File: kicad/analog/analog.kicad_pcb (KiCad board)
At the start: 4 copper layers, 75 x 50 mm, 85 parts, among them J101 FCI 20021221-00014T4LF, J301 CONN_02X05, Q201 DMG3414U, Q501 DMG3414U, Q601 DMG3414U, Q701 DMG3414U, U101 NCP694-3.3, U201 LTC2052, U202 ADS1220, U301 SP3003-04, U401 REF5030, U501 LTC2052, U502 ADS1220, U601 LTC2052, U602 ADS1220, U701 LTC2052, U702 ADS1220

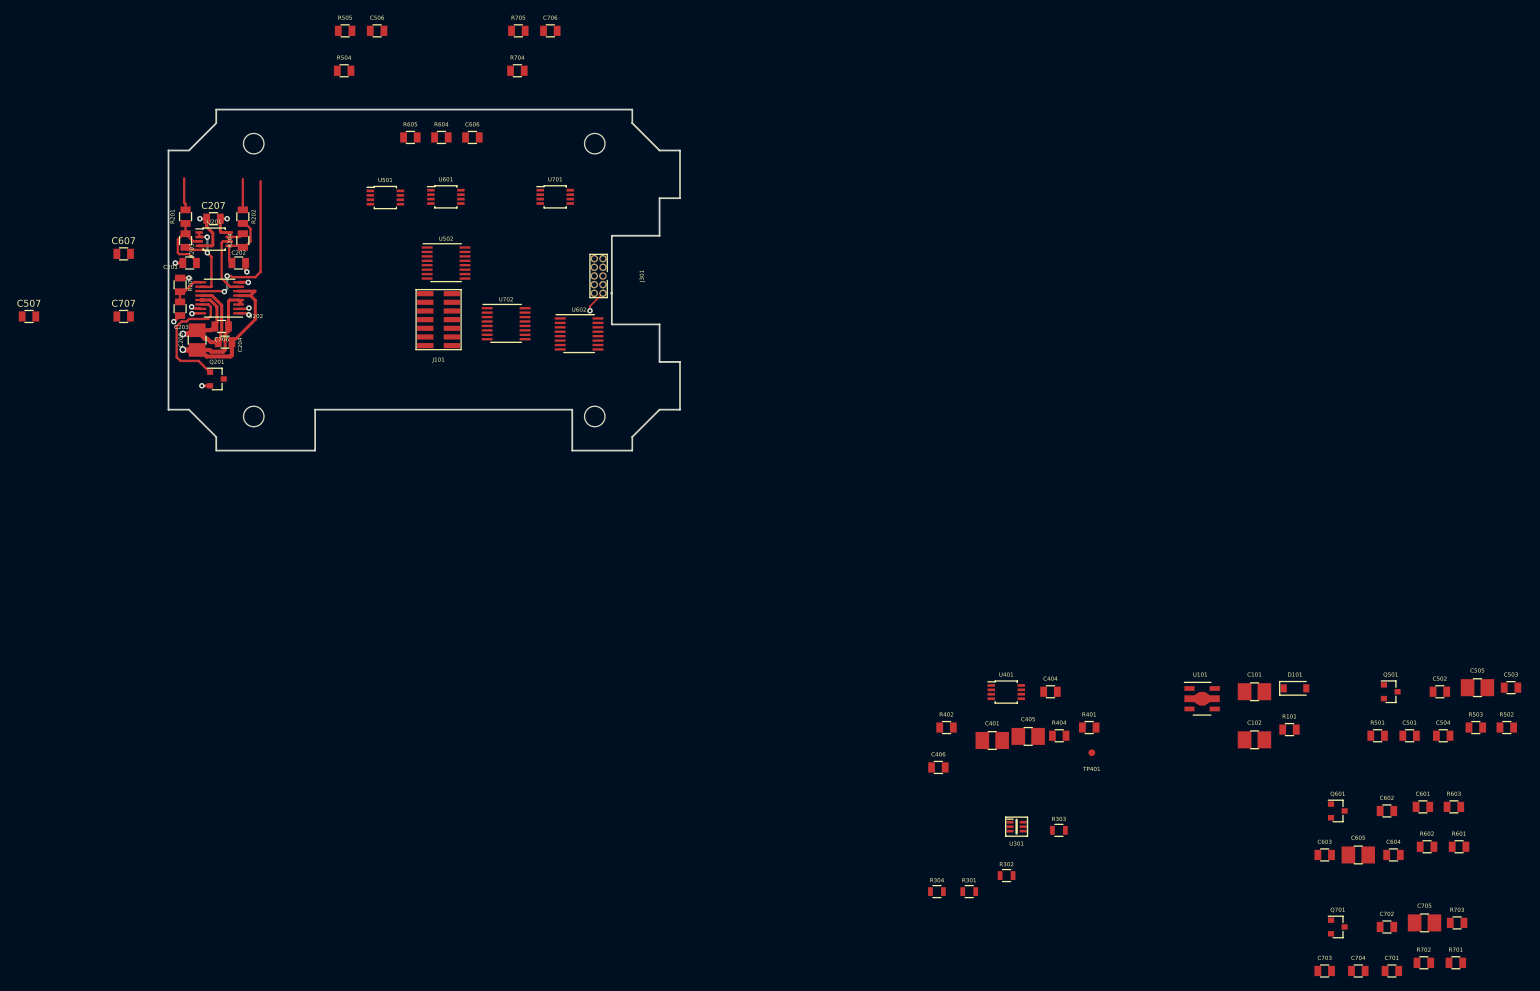
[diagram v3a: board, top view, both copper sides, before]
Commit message: analog routed DRC passes
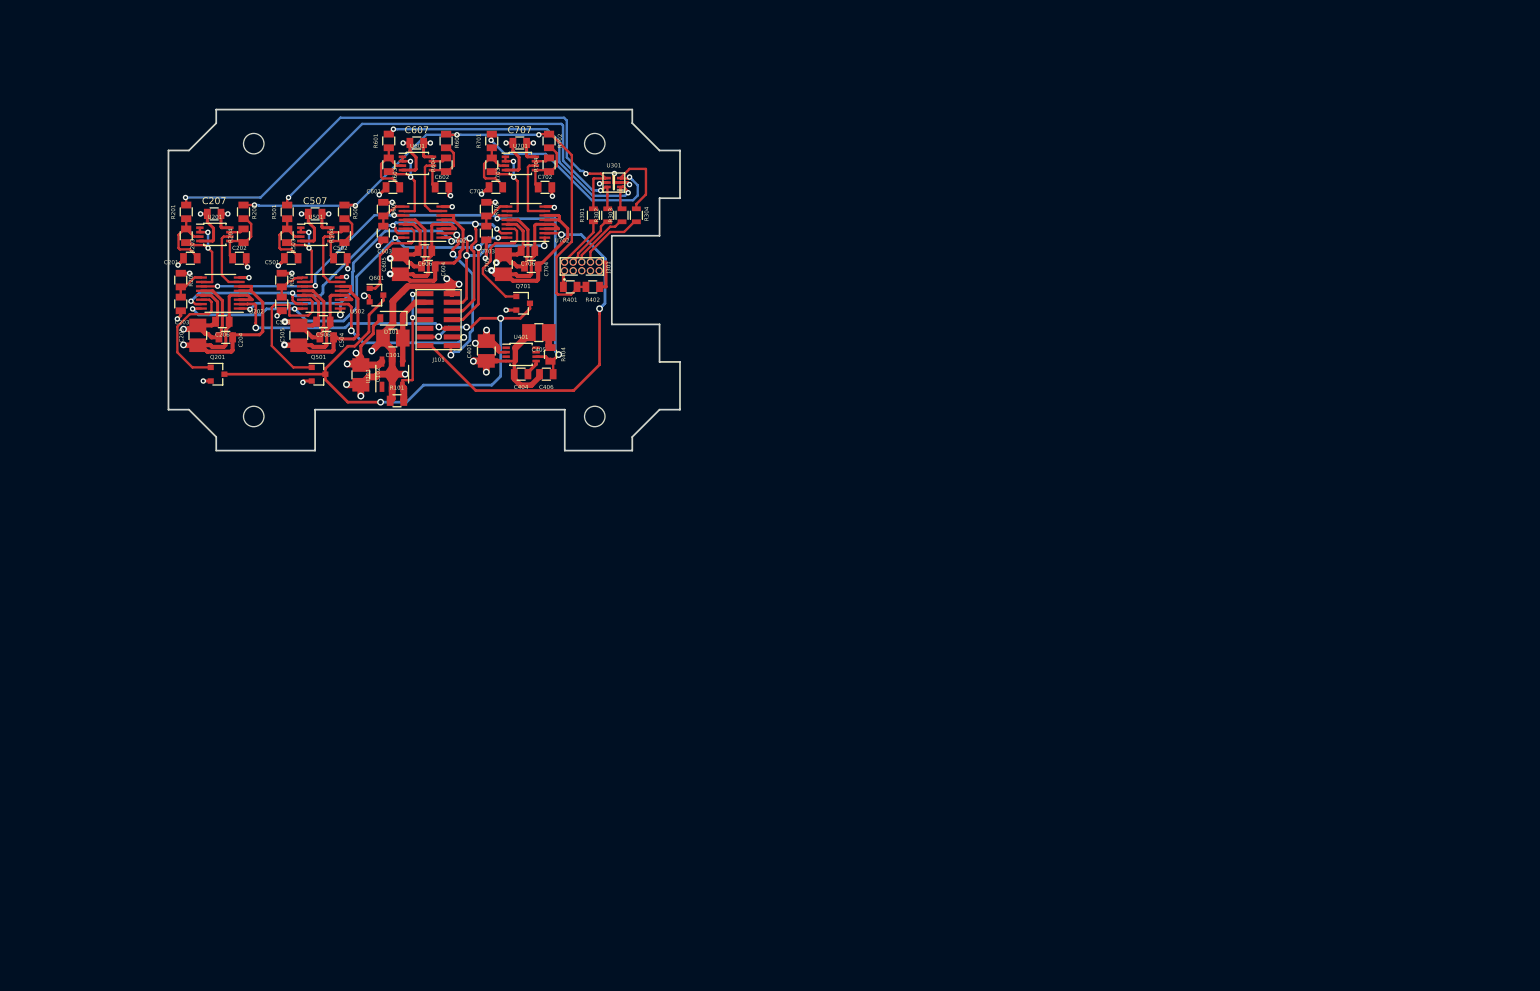
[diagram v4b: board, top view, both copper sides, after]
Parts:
- removed TP401: VREF, paddle:tp_th_1mm
- moved C503 188.8 mm to (16.6, 28.5), turned to 270 degrees
- moved R503 188.6 mm to (17.4, 18.5), turned to 270 degrees
- moved R601 188.0 mm to (32.3, 4.60), turned to 90 degrees
- moved R502 186.4 mm to (25.8, 15.0), turned to 90 degrees
- moved R701 185.7 mm to (47.4, 4.60), turned to 90 degrees
- moved R603 182.3 mm to (32.3, 8.10), turned to 270 degrees
- moved C505 180.4 mm to (19.1, 33.1), turned to 270 degrees
- moved R703 180.0 mm to (47.4, 8.10), turned to 270 degrees
- moved C501 178.3 mm to (18.0, 21.8)
- moved R501 177.4 mm to (17.4, 15.0), turned to 90 degrees
- moved R602 177.2 mm to (40.7, 4.60), turned to 90 degrees
- moved C601 176.2 mm to (32.9, 11.4)
- moved R702 176.0 mm to (55.8, 4.60), turned to 90 degrees
- moved C701 174.5 mm to (48.0, 11.4)
- moved C504 173.8 mm to (23.2, 33.4), turned to 180 degrees
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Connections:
- U301 pad 1: /IN_3 -> /IN_2
- U301 pad 3: /IN_2 -> /IN_3
- U301 pad 4: /IN_1 -> /IN_0
- U301 pad 6: /IN_0 -> /IN_1
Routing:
- net GND: track 53.1 -> 305.3 mm, vias 7 -> 38
- net +3.3VA: track 34.5 -> 147.2 mm, vias 4 -> 17
- net /PIO_B_BUSY*: track 0.00 -> 86.3 mm, vias 0 -> 4
- net /BRIDGE_COMP: track 4.50 -> 83.2 mm, vias 0 -> 4
- net /IN_0: track 4.68 -> 80.9 mm, vias 0 -> 2
- net /SPI_MISO: track 1.46 -> 75.0 mm, vias 1 -> 5
- net /SPI_MOSI: track 1.31 -> 73.4 mm, vias 1 -> 5
- net /SPI_SCLK: track 1.62 -> 70.9 mm, vias 1 -> 6
- net /VREF: track 24.6 -> 89.2 mm, vias 2 -> 5
- net /IN_1: track 0.00 -> 63.2 mm, vias 0 -> 2
- net /AN3_CS*: track 0.00 -> 56.3 mm, vias 0 -> 2
- net /IN_2: track 0.00 -> 46.5 mm, vias 0 -> 2
- net /IN_3: track 0.00 -> 41.8 mm, vias 0 -> 2
- net /AN0_CS*: track 1.58 -> 35.1 mm, vias 1 -> 2
- net /AN2_CS*: track 0.00 -> 24.7 mm, vias 0 -> 3
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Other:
- outline, holes or cut-outs redrawn

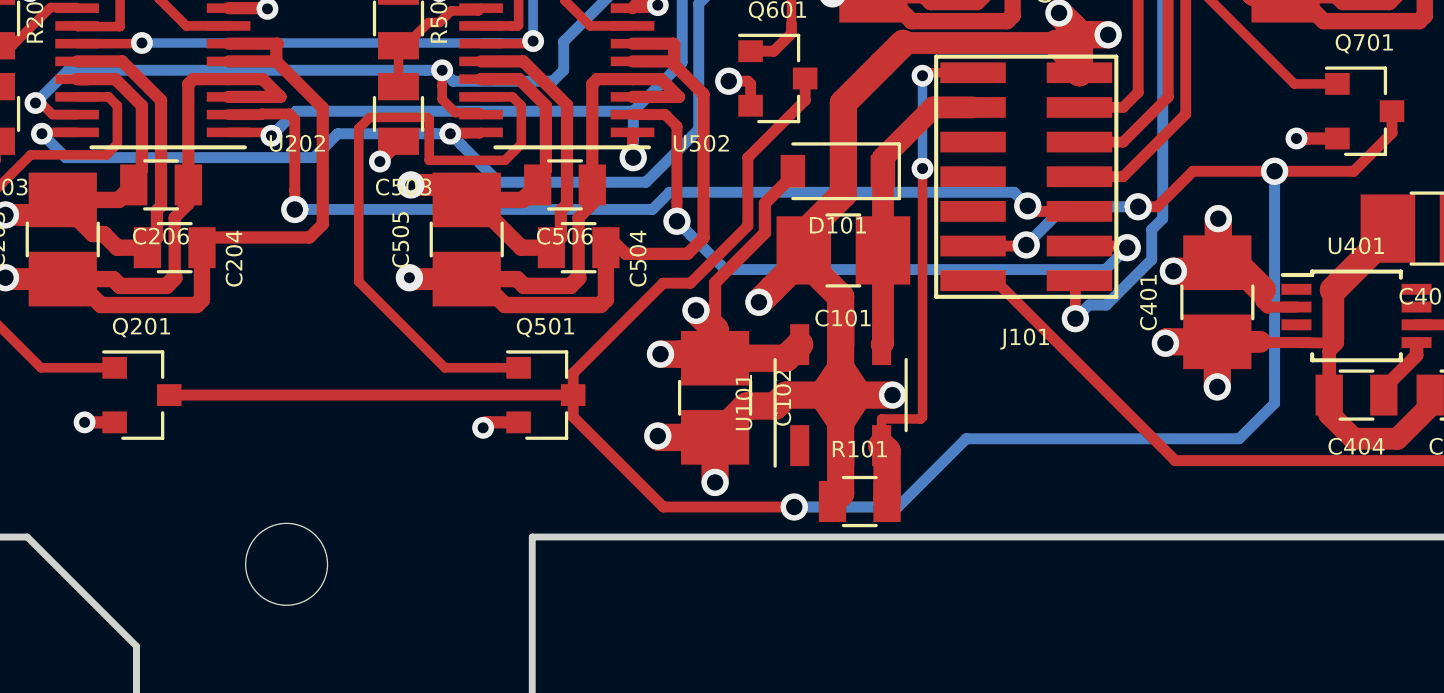
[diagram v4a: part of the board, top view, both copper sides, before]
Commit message: add bulk caps to analog
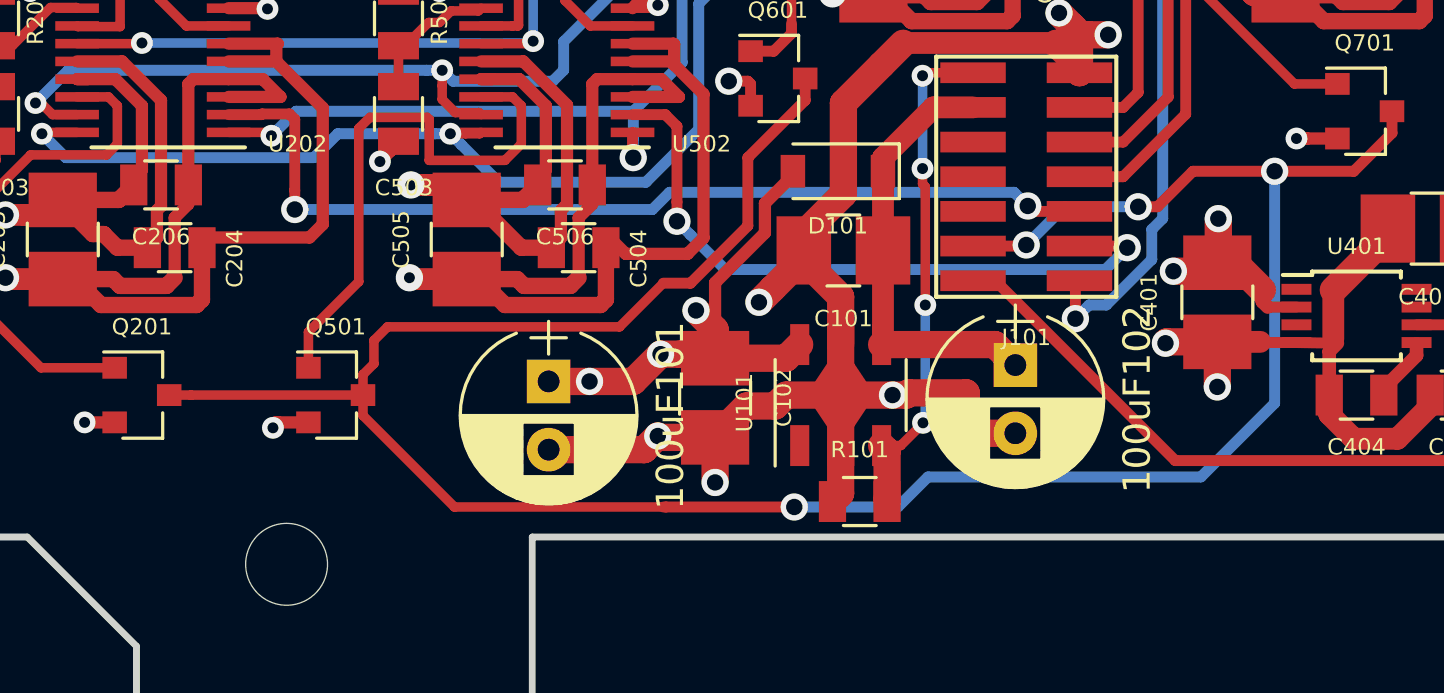
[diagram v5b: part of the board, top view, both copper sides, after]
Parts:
- added 100uF101: CP, paddle:CP_Radial_D6.3mm_P2.50mm, F.Cu at (22.1, 38.3)
- added 100uF102: CP, paddle:CP_Radial_D6.3mm_P2.50mm, F.Cu at (39.2, 37.7)
- moved Q501 7.70 mm to (14.3, 38.8)
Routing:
- net GND: track 305.3 -> 315.5 mm, vias 38 -> 39
- net /PIO_B_BUSY*: track 86.3 -> 94.6 mm
- net /+V_UNREG_SW: track 10.9 -> 16.1 mm
- net +3.3VA: track 147.2 -> 151.8 mm, vias 17 -> 18
- net Net-(Q501-Pad1): track 23.7 -> 20.4 mm
- net /+3.3V_AN_ENABLE: track 19.0 -> 18.9 mm, vias 2 -> 4

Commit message: Analog board and second rev processor board as sent to Goldphoenix
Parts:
- removed 100uF101, 100uF102: CP, paddle:CP_Radial_D6.3mm_P2.50mm
- added C103: 100uF, paddle:CP_Radial_D6.3mm_P2.50mm, F.Cu at (39.3, 37.8)
- added C104: 100uF, paddle:CP_Radial_D6.3mm_P2.50mm, F.Cu at (22.0, 38.3)
